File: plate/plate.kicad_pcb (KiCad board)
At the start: 2 copper layers, 223.1 x 76 mm, 6 parts

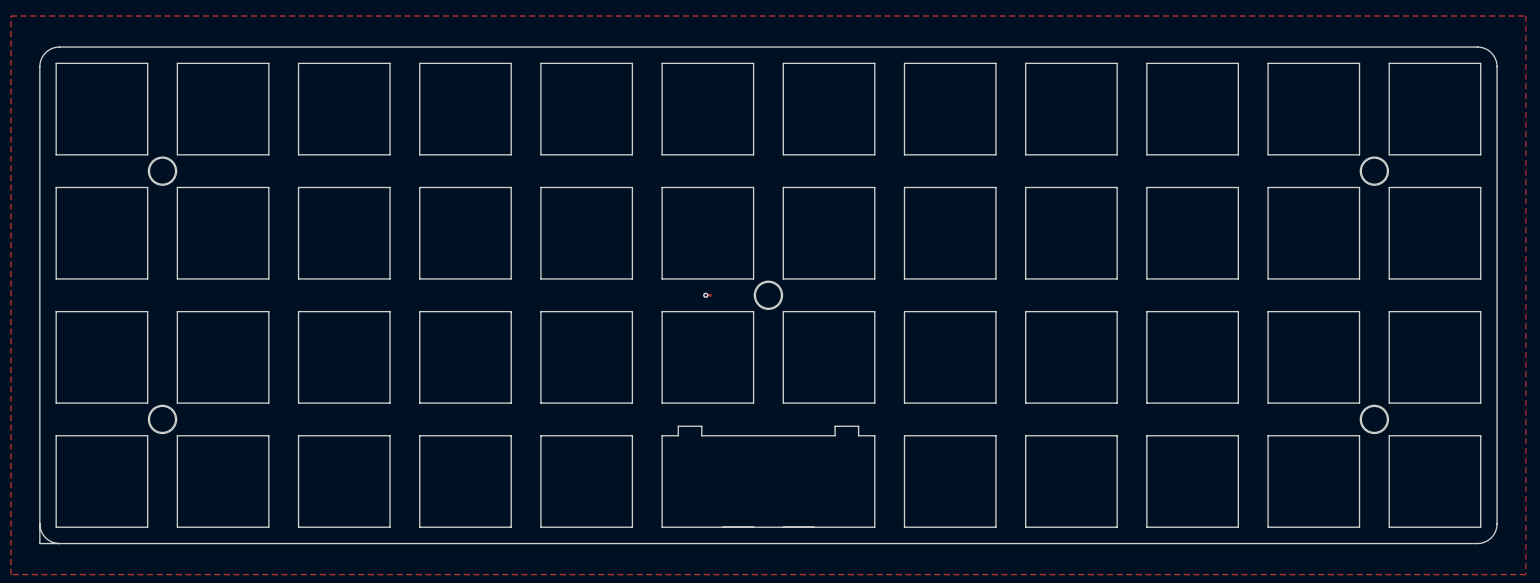
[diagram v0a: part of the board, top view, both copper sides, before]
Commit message: updating plate to 13.8x13.8mm
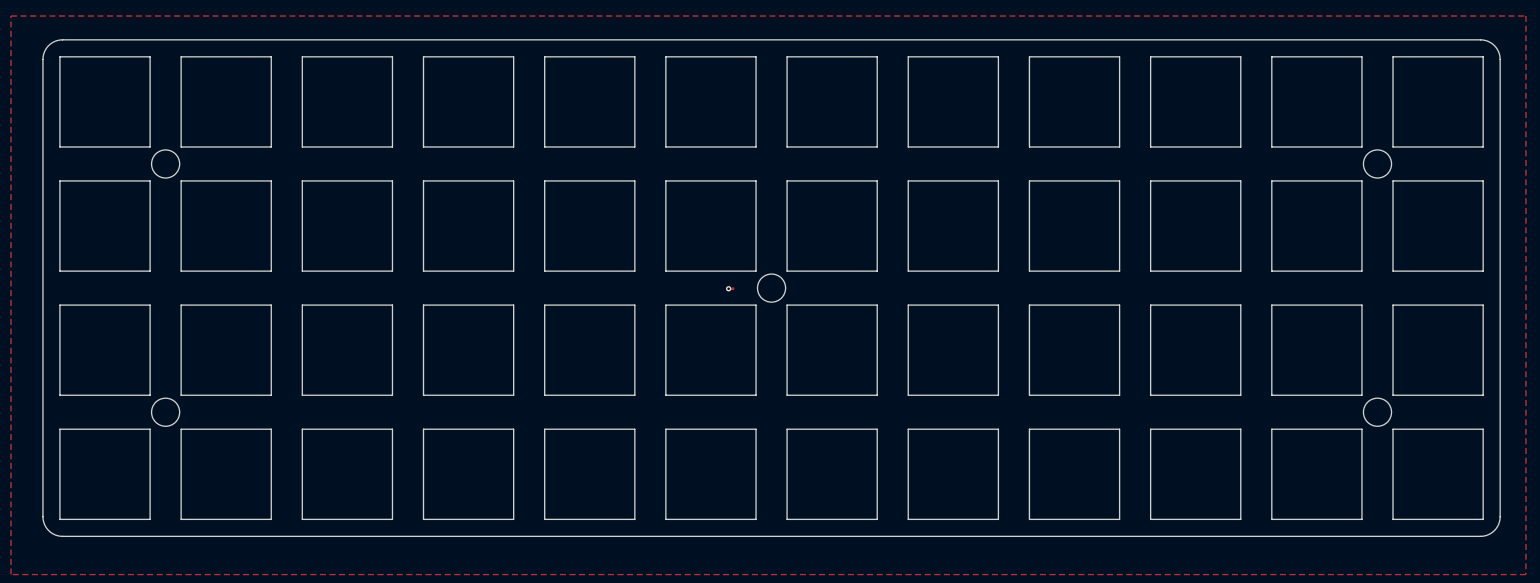
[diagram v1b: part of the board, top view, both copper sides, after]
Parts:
- moved   186.0 mm to (253.2, 77.4)
- moved   94.0 mm to (67.7, 115.4)
- moved   94.0 mm to (160.4, 96.4)
- moved   39.1 mm to (67.7, 77.4)
- moved   3.64 mm to (154.2, 96.5)
- moved   1.20 mm to (253.2, 115.4)
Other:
- board size 223.1 x 76 mm -> 223 x 76 mm
